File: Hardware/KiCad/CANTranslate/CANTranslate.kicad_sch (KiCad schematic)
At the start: 43 parts, among them J1 USB_C_Receptacle_USB2.0_16P, J2 Conn_01x05_Pin, J3 SM04B-GHS-TB(LF)(SN), J4 SM04B-GHS-TB(LF)(SN), SW1 SW_Push, SW2 SW_SPDT, SW3 SW_SPST, U1 USBLC6-2SC6, U2 STM32F103C8T6, U3 AMS1117-3.3, U4 TPS2116DRL, U5 SN65HVD230, Y1 16MHz

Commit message: Updated MCU from STM32F103C8T6 to STM32F303CCT6
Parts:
- U2: value STM32F103C8T6 -> STM32F303CCT6; symbol MCU_ST_STM32F1:STM32F103C8Tx -> MCU_ST_STM32F3:STM32F303CCTx; LCSC C8734 -> C81523
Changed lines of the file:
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@@
 	)
 	(symbol
-		(lib_id "MCU_ST_STM32F1:STM32F103C8Tx")
+		(lib_id "MCU_ST_STM32F3:STM32F303CCTx")
 		(at 90.17 76.2 0)
 		(unit 1)
@@
 			)
 		)
-		(property "Value" "STM32F103C8T6"
-			(at 94.234 115.824 0)
+		(property "Value" "STM32F303CCT6"
+			(at 94.996 116.332 0)
 			(effects
 				(font
@@
 			)
 		)
-		(property "Datasheet" "https://www.st.com/resource/en/datasheet/stm32f103c8.pdf"
+		(property "Datasheet" "https://www.st.com/resource/en/datasheet/stm32f303cc.pdf"
 			(at 90.17 76.2 0)
 			(effects
@@
 			)
 		)
-		(property "Description" "STMicroelectronics Arm Cortex-M3 MCU, 64KB flash, 20KB RAM, 72 MHz, 2.0-3.6V, 37 GPIO, LQFP48"
+		(property "Description" "STMicroelectronics Arm Cortex-M4 MCU, 256KB flash, 48KB RAM, 72 MHz, 2.0-3.6V, 37 GPIO, LQFP48"
 			(at 90.17 76.2 0)
 			(effects
@@
 			)
 		)
-		(property "LCSC" " C8734"
+		(property "LCSC" "C81523"
 			(at 90.17 76.2 0)
 			(effects

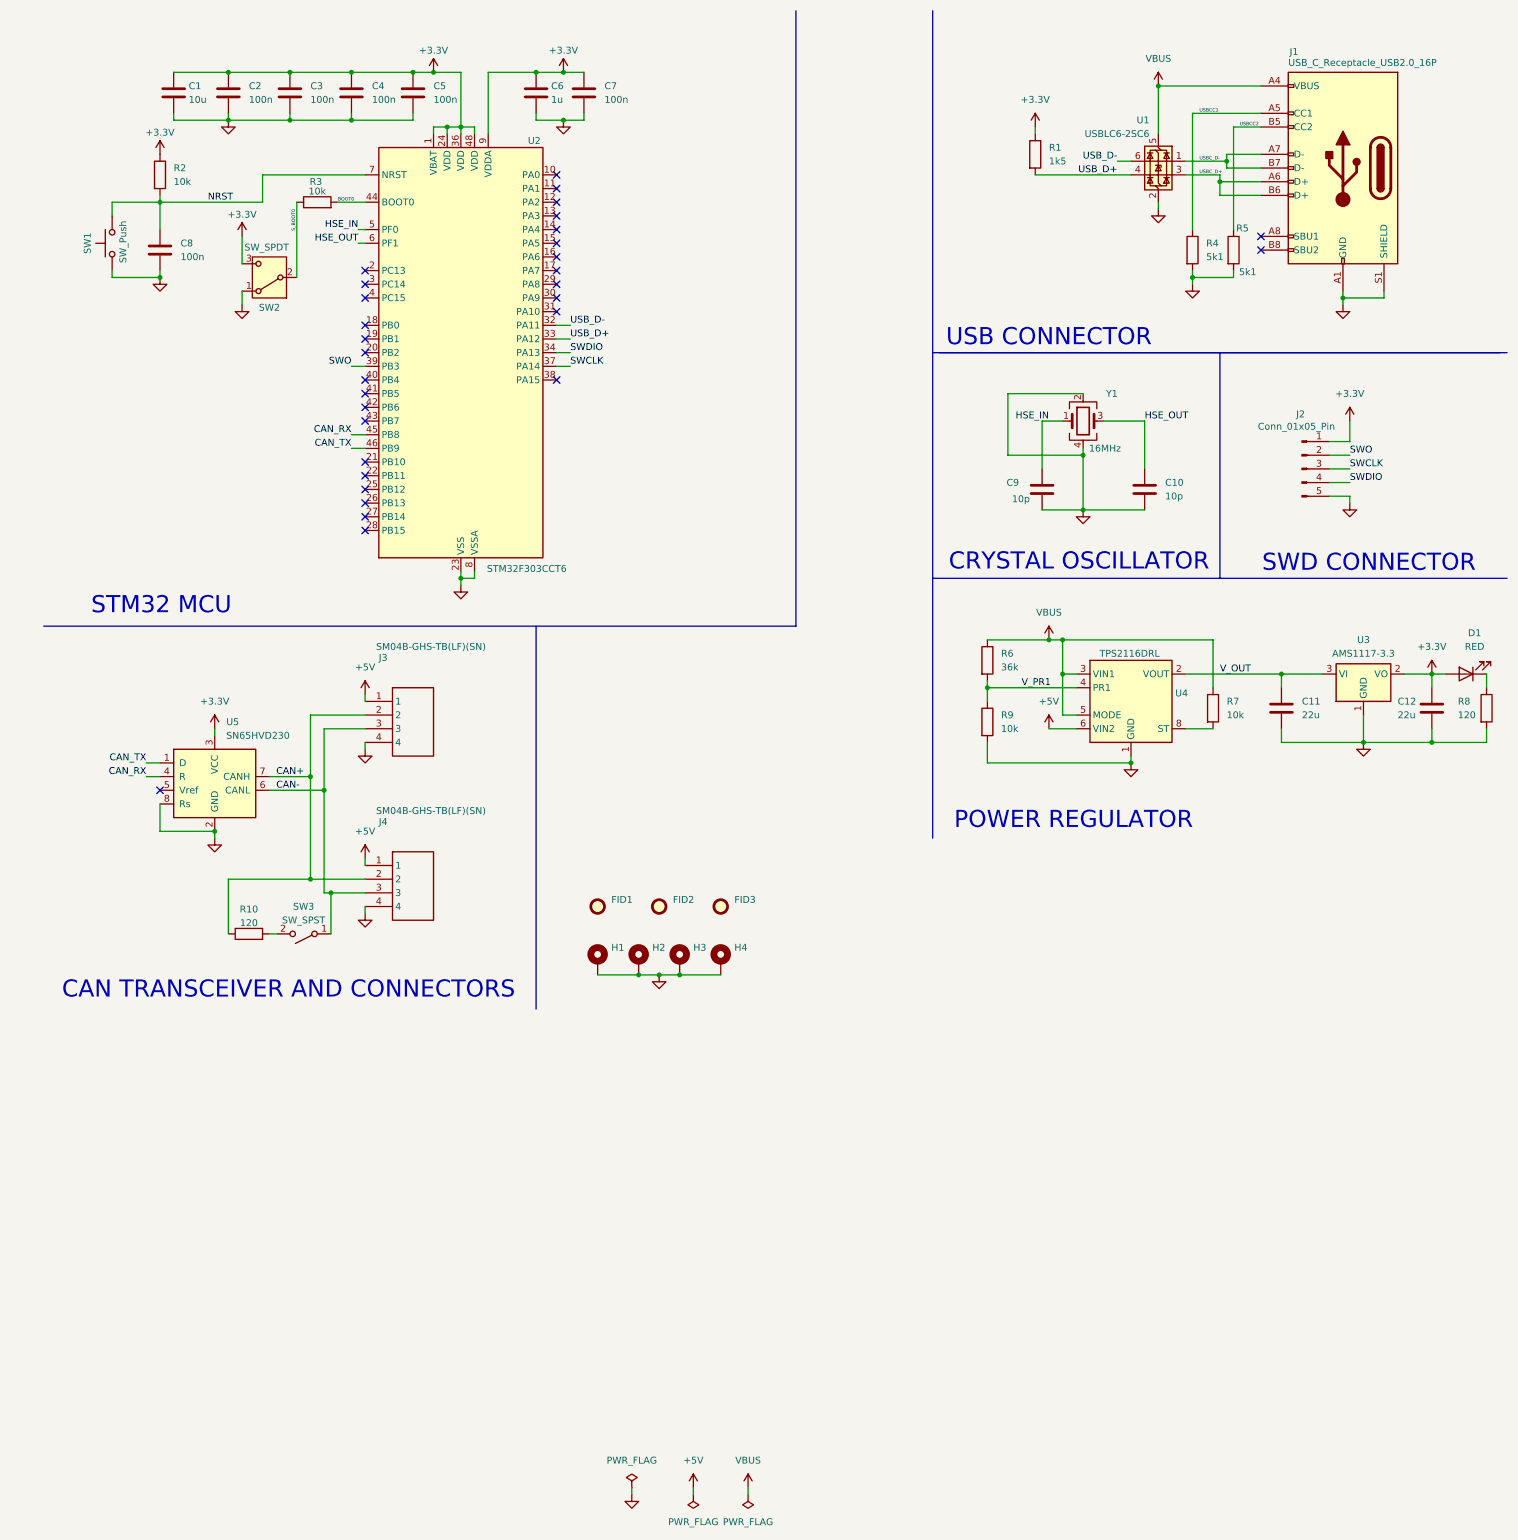
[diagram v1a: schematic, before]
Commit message: updated schematic to use two seprate CAN networks and different STM
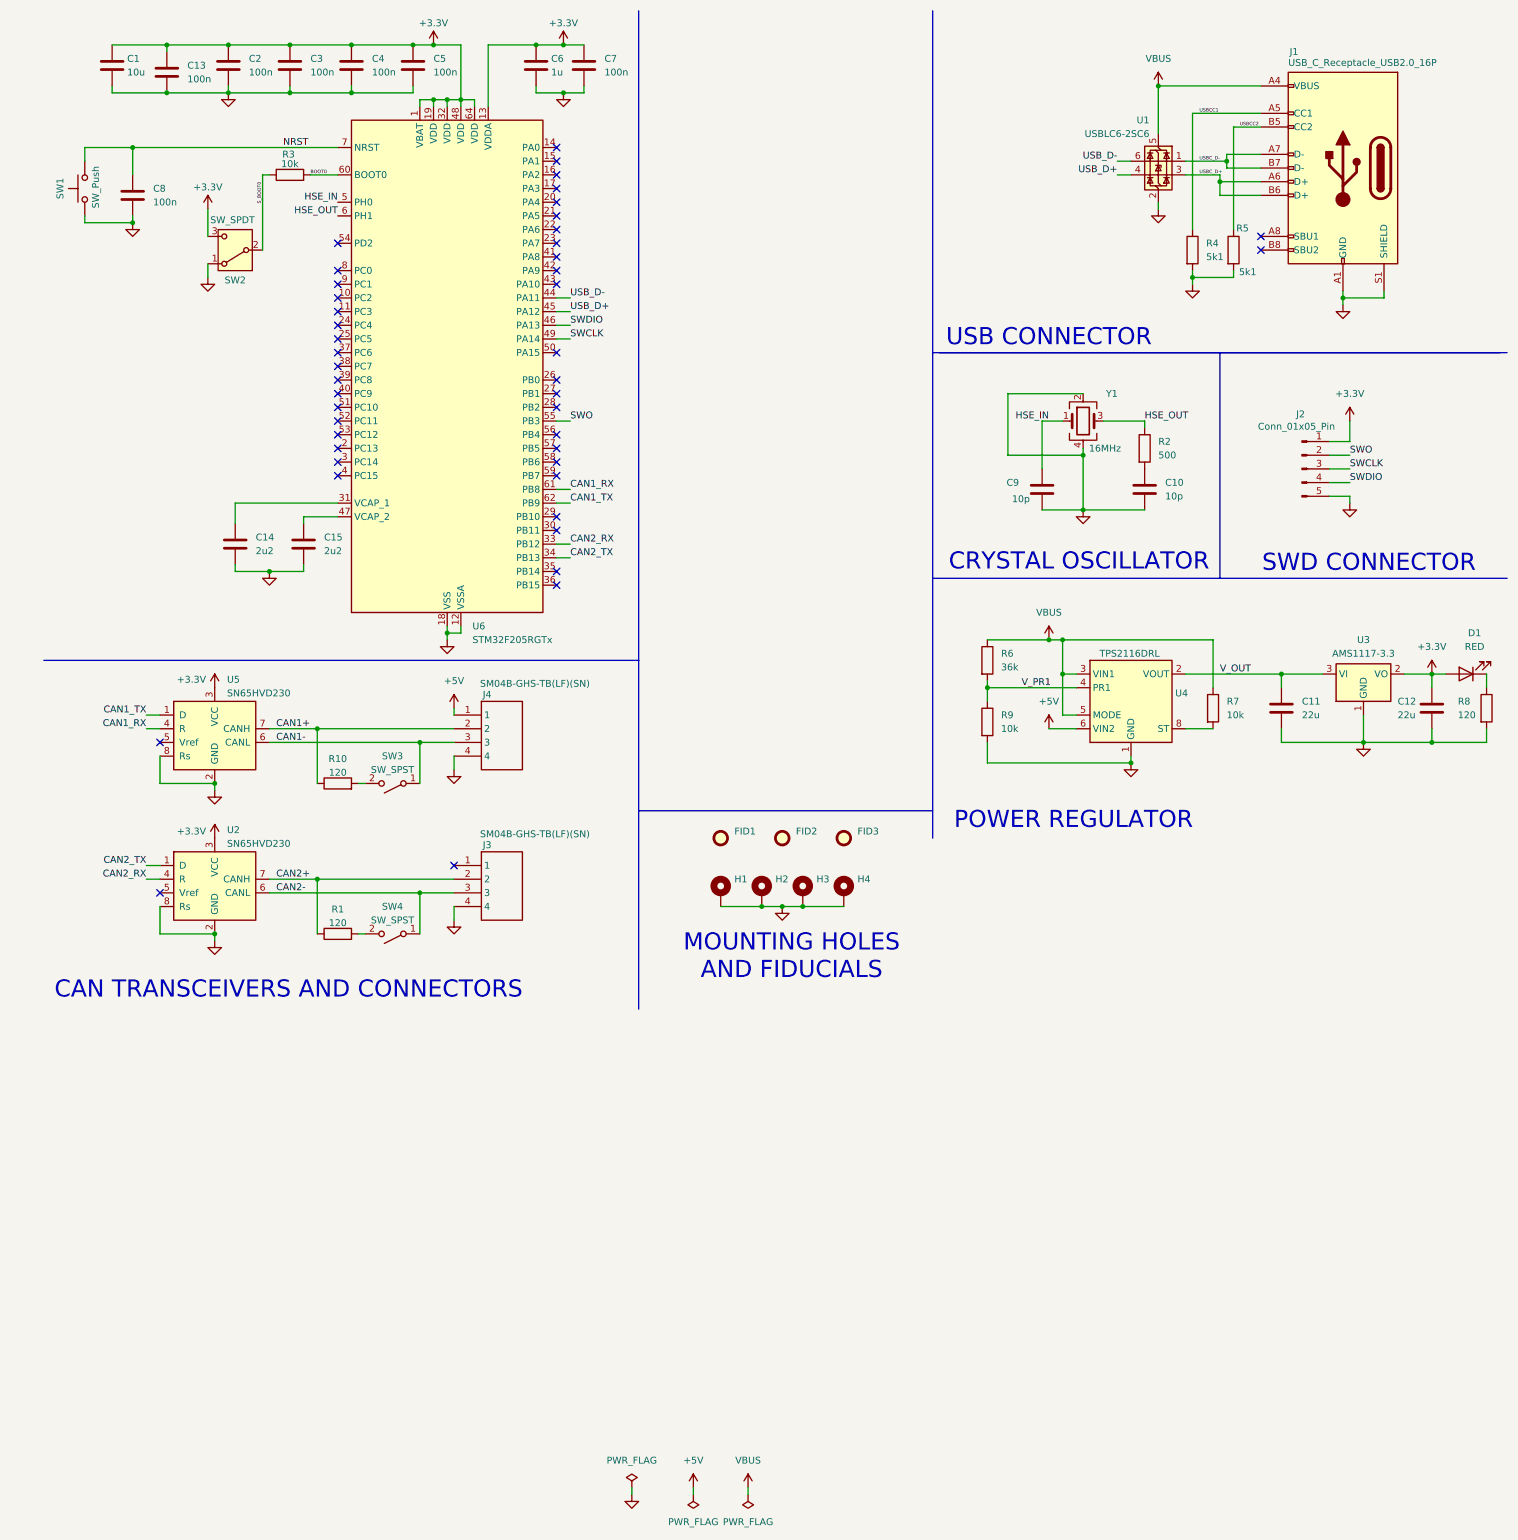
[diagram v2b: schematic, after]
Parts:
- removed U2: STM32F303CCT6, Package_QFP:LQFP-48_7x7mm_P0.5mm, symbol MCU_ST_STM32F3:STM32F303CCTx
- added C13: 100n, Capacitor_SMD:C_0402_1005Metric, symbol Device:C
- added C14, C15: 2u2, Capacitor_SMD:C_0402_1005Metric, symbol Device:C
- added SW4: SW_SPST, DSIC01LSGET:SW-SMD_DSIC01LSGET, symbol Switch:SW_SPST
- added U2: SN65HVD230, Package_SO:SOIC-8_3.9x4.9mm_P1.27mm, symbol Interface_CAN_LIN:SN65HVD230
- added U6: STM32F205RGTx, Package_QFP:LQFP-64_10x10mm_P0.5mm, symbol MCU_ST_STM32F2:STM32F205RGTx
- R1: value 1k5 -> 120; LCSC C25867 -> C25079
- R2: value 10k -> 500
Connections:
- net +3.3V: now also C13.1, U2.3 (VCC), U6.1 (VBAT), U6.13 (VDDA), U6.19 (VDD), U6.32 (VDD), U6.48 (VDD), U6.64 (VDD); no longer R1.1, R2.1
- net +5V: no longer J3.1
- net BOOT0: now also U6.60 (BOOT0)
- net GND: now also C13.2, C14.2, C15.2, U2.2 (GND), U2.8 (Rs), U6.12 (VSSA), U6.18 (VSS), U6.63 (VSS)
- net HSE_IN: now also U6.5 (PH0)
- net HSE_OUT: now also R2.1, U6.6 (PH1); no longer C10.1
- net NRST: now also U6.7 (NRST); no longer R2.2
- net SWCLK: now also U6.49 (PA14)
- net SWDIO: now also U6.46 (PA13)
- net SWO: now also U6.55 (PB3)
- net USB_D+: now also U6.45 (PA12); no longer R1.2
- net USB_D-: now also U6.44 (PA11)
- net CAN+ renamed CAN1+
- net CAN1+: no longer J3.2
- net CAN- renamed CAN1-
- net CAN1-: no longer J3.3
- net CAN_RX renamed CAN1_RX
- net CAN1_RX: now also U6.61 (PB8)
- net CAN_TX renamed CAN1_TX
- net CAN1_TX: now also U6.62 (PB9)
- new net: C15.1, U6.47 (VCAP_2)
- new net: C10.1, R2.2
- new net: C14.1, U6.31 (VCAP_1)
- new net: R1.2, SW4.2 (B)
- new net CAN2+: J3.2, R1.1, U2.7 (CANH)
- new net CAN2-: J3.3, SW4.1 (A), U2.6 (CANL)
- new net CAN2_RX: U2.4 (R), U6.33 (PB12)
- new net CAN2_TX: U2.1 (D), U6.34 (PB13)
- no-connect marks 31 -> 45
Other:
- note added: "CAN TRANSCEIVERS AND CONNECTORS"
- note added: "MOUNTING HOLES AND FIDUCIALS"
- note removed: "CAN TRANSCEIVER AND CONNECTORS"
- note removed: "STM32 MCU"
- moved on the sheet: C1, C2, C3, C4, C5, C6, C7, C8, FID1, FID2, FID3, H1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

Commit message: More Hardware Updates
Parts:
- C12: renamed from C14; LCSC C1525 -> C12530
- C13: renamed from C15; LCSC C1525 -> C12530
- R4: renamed from R2; value 500 -> 470; LCSC C25744 -> C25117
- SW2: footprint Button_Switch_THT:SW_Slide_SPDT_Straight_CK_OS102011MS2Q -> easyeda2kicad:SW-TH_SS12D07VG4; LCSC C221829 -> C2939726
- U2: renamed from U6; value STM32F205RGTx -> STM32F205RGT6; LCSC (none) -> C30481
- renumbered C9 to C10, C10 to C11, C11 to C14, C12 to C15, C13 to C2, C2 to C3, C3 to C4, C4 to C5, C5 to C6, C6 to C7, C7 to C8, C8 to C9, J4 to J3, J3 to J4, R3 to R1, R1 to R10, R4 to R2, R5 to R3, R6 to R5, R7 to R6, R8 to R7, R9 to R8, R10 to R9, U2 to U6
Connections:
- net +5V: now also J4.1; no longer J3.1
- net VCAP_2: now reaches C13.1, U2.47 (VCAP_2)
- net VCAP_1: now reaches C12.1, U2.31 (VCAP_1)
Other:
- moved on the sheet: C12, C13, C2
